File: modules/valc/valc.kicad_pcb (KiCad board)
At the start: 2 copper layers, 40.6 x 40.6 mm, 42 parts, among them J1 2, J10 11, J11 12, J12 13, J13 A0, J14 A1, J15 A2, J16 A3, J17 A4, J18 A5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

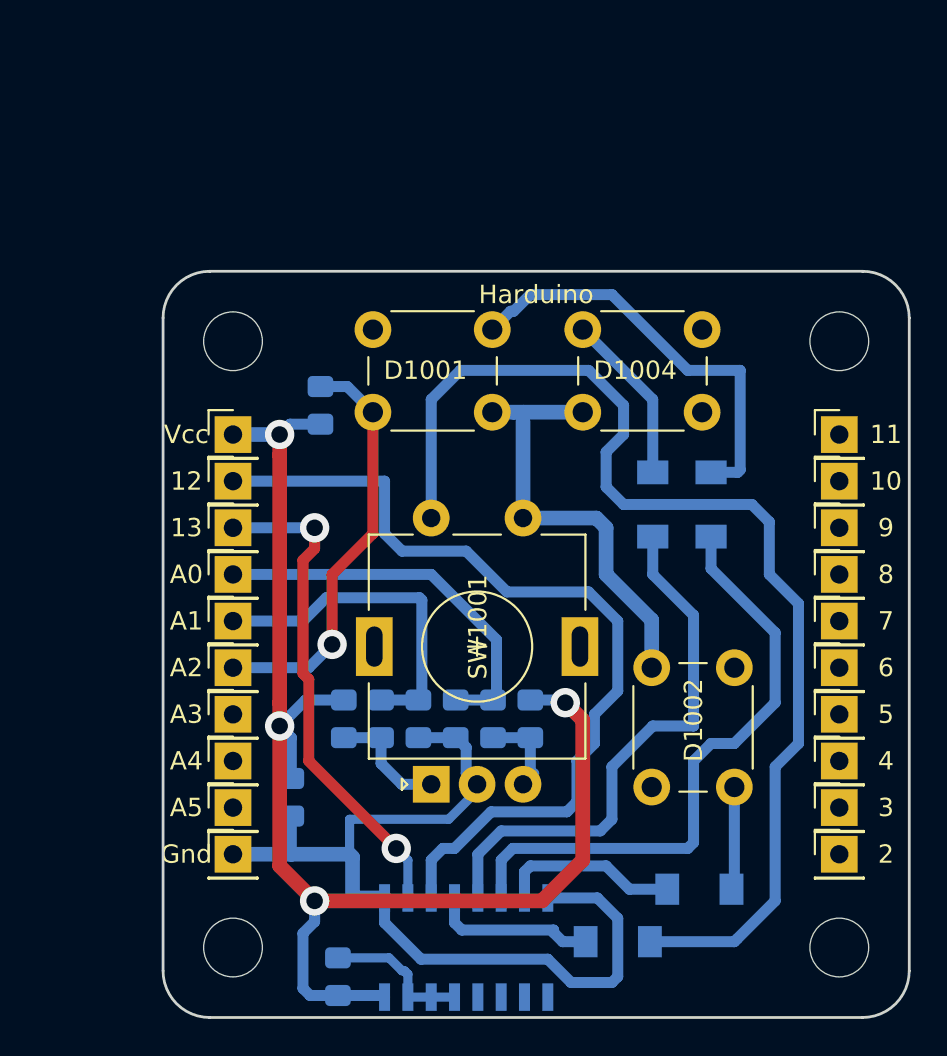
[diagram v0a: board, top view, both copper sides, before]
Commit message: Center pcb. Add photomask in pdf.
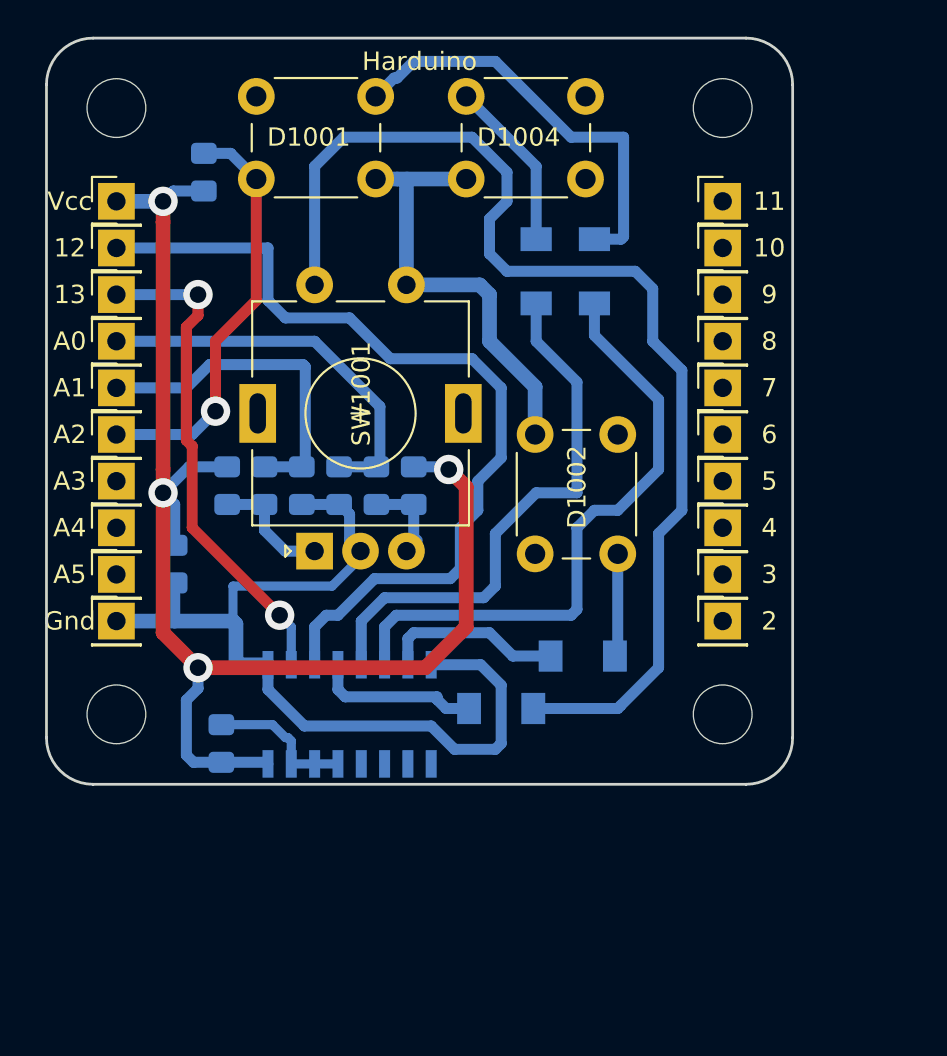
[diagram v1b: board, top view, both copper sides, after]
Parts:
- moved J4 14.2 mm to (119.4, 62.2)
- moved C3 14.2 mm to (89.5, 66.7)
- moved D1 14.2 mm to (107.3, 74.6)
- moved D1004 14.2 mm to (105.4, 41.3)
- moved D3 14.2 mm to (112.4, 50.8)
- moved H3 14.2 mm to (119.4, 41.9)
- moved J1 14.2 mm to (119.4, 69.8)
- moved J16 14.2 mm to (86.4, 62.2)
- moved J2 14.2 mm to (119.4, 67.3)
- moved J3 14.2 mm to (119.4, 64.8)
- moved J5 14.2 mm to (119.4, 59.7)
- moved J7 14.2 mm to (119.4, 54.6)
- moved D1001 14.2 mm to (94.0, 41.3)
- moved D1002 14.2 mm to (113.7, 59.7)
- moved D2 14.2 mm to (109.2, 50.8)
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
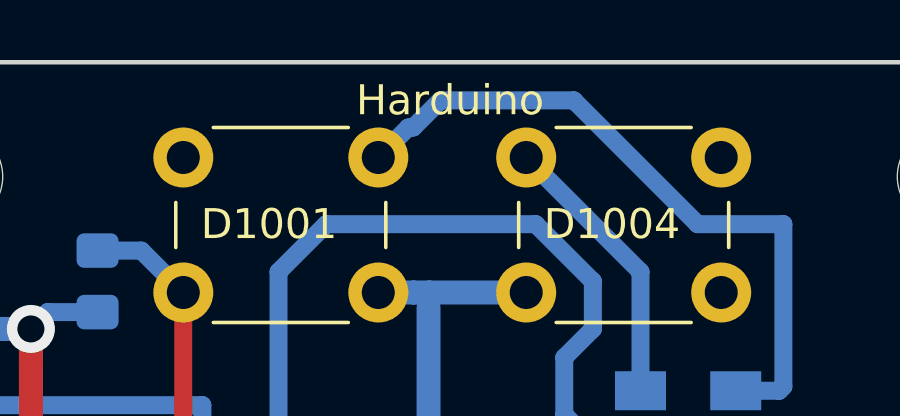
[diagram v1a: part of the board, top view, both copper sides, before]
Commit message: Harduino -> HardDuino
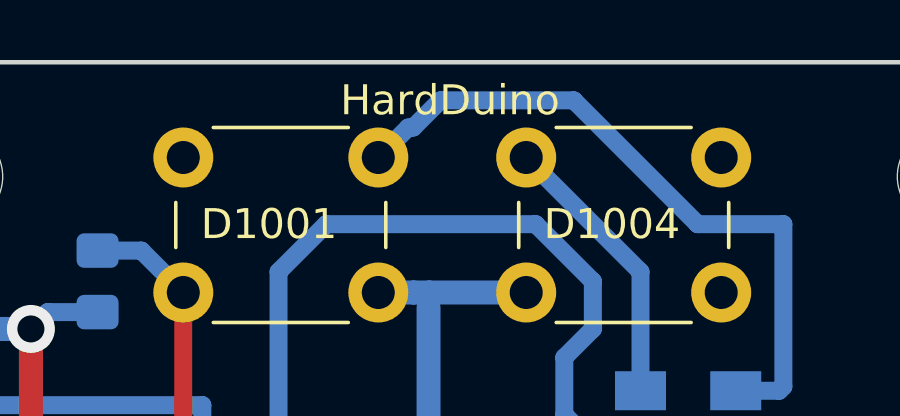
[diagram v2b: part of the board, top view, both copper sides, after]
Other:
- board text added: "HardDuino"
- board text removed: "Harduino"
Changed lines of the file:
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@@
     )
   )
-  (gr_text Harduino (at 102.87 39.37) (layer F.SilkS)
+  (gr_text HardDuino (at 102.87 39.37) (layer F.SilkS)
     (effects (font (size 1 1) (thickness 0.15)))
   )

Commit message: Fix pullup
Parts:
- R6: value 5k -> 10k
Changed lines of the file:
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@@
       (effects (font (size 1 1) (thickness 0.15)) (justify mirror))
     )
-    (fp_text value 5k (at 0 -1.65 90) (layer B.Fab)
+    (fp_text value 10k (at 0 -1.65 90) (layer B.Fab)
       (effects (font (size 1 1) (thickness 0.15)) (justify mirror))
     )
